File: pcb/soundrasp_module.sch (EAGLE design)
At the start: 65 parts, among them IC1 74HC165D, IC2 ULN2003AD, SW1 EC12E_SW, SW2 EC12E_SW

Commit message: Refactoring scema and doing initial pcb layout.
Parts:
- removed BACKLIGHT_LED, KNOB_LED: LED, SparkFun:LED-TRICOLOR-THROUGHHOLE
- removed C10, C12: 1uF, rcl:C-EUC0805
- removed IC2: ULN2003AD, uln-udn:ULN2003AD
- removed INDICATOR_SHIFT: 74HC595D, 74xx-eu:74HC595D
- removed JP1: (no value), SparkFun:M02LOCK_LONGPADS
- removed LED1, LED14, LED15, LED16, LED17, LED18, LED19, LED2: WS2812B, WS2812:WS2812B
- removed LED10, LED11, LED12, LED13, LED9: (no value), led:LEDCHIPLED_0805
- removed OS1, OS2: (no value), tcrt5000:TCRT5000
- removed R10, R11, R12, R13, R8, R9: (no value), rcl:R-EU_R0805
- removed R2, R3, R4, R5, R6, R7: 10k, rcl:R-EU_R0805
- removed R38, R41: 100k, rcl:R-EU_R0805
- removed R42, R43: 200 Ohm, rcl:R-EU_R0805
- removed R45, R46, R47, R48: 220, rcl:R-EU_R0805
- removed S1: (no value), SparkFun:TAC_SWITCHPTH
- removed SW2: EC12E_SW, switch-alps:EC12E_SW
- removed U$1: CHARACTER_LCD_8X2RT0802, character_lcd_RT0802B-1:CHARACTER_LCD_8X2RT0802
- added BAR1, BAR10, BAR2, BAR3, BAR4, BAR5, BAR6, BAR7, BAR8, BAR9, MODE_LED, TOGGLE_LED, WHEEL_LED: WS2812B, WS2812:WS2812B
- added DISPLAY: M16LOCK, SparkFun-Connectors:M16LOCK
- added FORCE_FEEDBACK: (no value), SparkFun:M02LOCK_LONGPADS
- added H1, H2, H3, H4: MOUNT-HOLE4.1, holes:MOUNT-HOLE4.1
- added IR_1, IR_2: (no value), SparkFun-LED:LED3MM
- added IR_SENSE_1, IR_SENSE_2: SFH205, opto-trans-siemens:SFH205
- added MENU_SWITCH, TOGGLE_SWITCH, WHEEL_SWITCH: SWITCH-MOMENTARY-2-SMD-1101NE, SparkFun-Electromechanical:SWITCH-MOMENTARY-2-SMD-1101NE
- added POWER_LED: (no value), led:LEDCHIPLED_0805
- added RN1: 220R, resistor-dil:4R-N0603-ARV
- added RN2, RN3: 10k, resistor-dil:4R-N0603-ARV
- added T1, T2: (no value), transistor:MMBT2222ALT1-NPN-SOT23-BEC
- R1: device pot:TRIM_EU-B25X -> rcl:R-TRIMM3296W
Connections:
- removed net N$14: BACKLIGHT_LED.RED, R8.2
- removed net N$18: KNOB_LED.BLU, R12.2
- removed net N$19: KNOB_LED.GRN, R13.2
- removed net N$24: INDICATOR_SHIFTA.QC, R10.1
- removed net N$25: INDICATOR_SHIFTA.QD, R11.1
- removed net N$29: LED1.DI, LED19.DO
- removed net N$74: OS2.ANODE, R42.2
- removed net N$75: INDICATOR_SHIFTA.SER, LCD_SHIFTA.QH*
- removed net N$76: INDICATOR_SHIFTA.QH*
- removed net N$79: OS1.ANODE, R43.2
- removed net N$81: INDICATOR_SHIFTA.QE, R12.1
- removed net N$82: INDICATOR_SHIFTA.QF, R13.1
- removed net N$83: IC2.I1, INDICATOR_SHIFTA.QG
- removed net N$84: IC2.I6, INDICATOR_SHIFTA.QH
- removed net N$85: IC2.I2, IC2.I3, LCD_SHIFTA.QG
- removed net N$88: IC2.I4, IC2.I5, LCD_SHIFTA.QH
- removed net N$89: IC2.O2, LED10.C
- removed net N$90: LED10.A, R45.1
- removed net N$91: IC2.O6, OS1.CATHODE, OS2.CATHODE
- removed net N$92: LED11.A, R46.1
- removed net N$93: IC2.O3, LED11.C
- removed net N$94: LED12.A, R47.1
- removed net N$95: LED13.A, R48.1
- removed net N$96: IC2.O4, LED12.C
- removed net N$97: IC2.O5, LED13.C
- removed net V+: R45.2, R46.2, R47.2, R48.2
- new net BAR7: BAR6.DO, BAR7.DI
- new net CONTRAST: DISPLAY.3, R1.S
- new net D4: DISPLAY.11, LCD_SHIFTA.QB
- new net D5: DISPLAY.12, LCD_SHIFTA.QC
- new net D6: DISPLAY.13, LCD_SHIFTA.QD
- new net D7: DISPLAY.14, LCD_SHIFTA.QE
- new net E: DISPLAY.6, LCD_SHIFTA.QA
- new net LED_COLORS_IN: TOGGLE_LED.DI, X1.5
- new net LED_COLORS_OUT: WHEEL_LED.DO, X2.5
- new net R/W: DISPLAY.5
- new net RS: DISPLAY.4, LCD_SHIFTA.QF
- net +5V: now also BAR1.VDD, BAR10.VDD, BAR2.VDD, BAR3.VDD, BAR4.VDD, BAR5.VDD, BAR6.VDD, BAR7.VDD, BAR8.VDD, BAR9.VDD, DISPLAY.15, DISPLAY.2, FORCE_FEEDBACK.1, MODE_LED.VDD, RN1C.1, RN1D.1, RN2A.2, RN2B.2, RN2C.2, RN2D.2, RN3A.2, RN3B.2, RN3C.2, RN3D.2, TOGGLE_LED.VDD, WHEEL_LED.VDD; no longer C10.1, C12.1, INDICATOR_SHIFTA.SCL, INDICATOR_SHIFTP.VCC, JP1.1, LED1.VDD, LED14.VDD, LED15.VDD, LED16.VDD, LED17.VDD, LED18.VDD, LED19.VDD, LED2.VDD, R2.2, R3.2, R38.2, R4.2, R41.2, R42.1, R43.1, R5.2, R6.2, R7.2, U$1.+5V
- net GND: now also BAR1.VSS, BAR10.VSS, BAR2.VSS, BAR3.VSS, BAR4.VSS, BAR5.VSS, BAR6.VSS, BAR7.VSS, BAR8.VSS, BAR9.VSS, DISPLAY.1, DISPLAY.16, IR_SENSE_1.C, IR_SENSE_2.C, MENU_SWITCH.1, MODE_LED.VSS, POWER_LED.C, T1.E, T2.E, TOGGLE_LED.VSS, TOGGLE_SWITCH.1, WHEEL_LED.VSS, WHEEL_SWITCH.1; no longer IC2.GND, INDICATOR_SHIFTA.G, INDICATOR_SHIFTP.GND, LED1.VSS, LED14.VSS, LED15.VSS, LED16.VSS, LED17.VSS, LED18.VSS, LED19.VSS, LED2.VSS, LED9.C, OS1.EMITTER, OS2.EMITTER, S1.2, SW2G$1.C, SW2G$2.2, U$1.GND, U$1.R/W
- net LED_VOLTAGE: no longer BACKLIGHT_LED.C, KNOB_LED.C, X1.5, X2.5
- net N$1: now also IR_1.A, RN1C.2; no longer R1.S, U$1.LCD_V+
- net N$10: now also BAR10.DI, BAR9.DO; no longer LCD_SHIFTA.QC, U$1.D5
- net N$11: now also BAR10.DO, WHEEL_LED.DI; no longer LCD_SHIFTA.QD, U$1.D6
- net N$12: now also MODE_LED.DI, TOGGLE_LED.DO; no longer LCD_SHIFTA.QE, U$1.D7
- net N$13: now also BAR1.DI, MODE_LED.DO; no longer LCD_SHIFTA.QF, U$1.RS
- net N$15: now also LCD_SHIFTA.QG, RN1A.1; no longer BACKLIGHT_LED.BLU, R9.2
- net N$16: now also RN1A.2, T1.B; no longer BACKLIGHT_LED.GRN, R10.2
- net N$17: now also LCD_SHIFTA.QH, RN1B.1; no longer KNOB_LED.RED, R11.2
- net N$2: now also RN2D.1; no longer R4.1
- net N$20: now also IR_1.C, IR_2.C, T2.C; no longer INDICATOR_SHIFTA.QA, R8.1
- net N$21: now also RN1B.2, T2.B; no longer INDICATOR_SHIFTA.QB, R9.1
- net N$22: now also BAR1.DO, BAR2.DI; no longer LED14.DO, LED15.DI
- net N$23: now also BAR2.DO, BAR3.DI; no longer LED15.DO, LED16.DI
- net N$26: now also BAR3.DO, BAR4.DI; no longer LED16.DO, LED17.DI
- net N$27: now also BAR4.DO, BAR5.DI; no longer LED17.DO, LED18.DI
- net N$28: now also BAR5.DO, BAR6.DI; no longer LED18.DO, LED19.DI
- net N$3: now also RN2C.1; no longer R5.1
- net N$30: now also BAR7.DO, BAR8.DI; no longer LED1.DO, LED2.DI
- net N$4: now also IR_SENSE_1.A, RN2A.1; no longer R6.1, SW2G$1.A
- net N$5: now also IR_SENSE_2.A, RN3D.1; no longer R7.1, SW2G$1.B
- net N$50: now also MENU_SWITCH.2, RN3B.1; no longer C10.2, OS2.COLLECTOR, R41.1
- net N$6: now also RN2B.1; no longer R2.1
- net N$7: now also RN3C.1, WHEEL_SWITCH.2; no longer R3.1, S1.4, SW2G$2.1
- net N$73: now also POWER_LED.A; no longer LED9.A
- net N$8: now also IR_2.A, RN1D.2; no longer LCD_SHIFTA.QA, U$1.ENABLE
- net N$80: now also RN3A.1, TOGGLE_SWITCH.2; no longer C12.2, OS1.COLLECTOR, R38.1
- net N$86: now also FORCE_FEEDBACK.2, T1.C; no longer IC2.O1, JP1.2
- net N$9: now also BAR8.DO, BAR9.DI; no longer LCD_SHIFTA.QB, U$1.D4
- net OUTPUT_CLOCK: no longer INDICATOR_SHIFTA.SCK
- net OUTPUT_LATCH: no longer INDICATOR_SHIFTA.RCK
- net OUTPUT_OUT: now also LCD_SHIFTA.QH*
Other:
- note added: "Character LCD display, 16x2"
- note added: "Mode Indicator"
- note added: "Optical Value Wheel"
- note added: "Power LED"
- note added: "Toggle Indicator"
- note added: "Value Indicator Bar"
- note added: "Wheel Light"
- note removed: "Backlight"
- note removed: "Edge Lighting"
- note removed: "Knob Light"
- note removed: "LCD 8x2"
- note removed: "Position Indicators"
- note removed: "Powerled"
- note removed: "Proximity Sensors"
- note removed: "Value Knob"
- moved on the sheet: C11, D1, IC1, IC1P, LCD_SHIFTP, R39, R40, R44, SW1, X1, X2

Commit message: Removed force feedback. Changed design to use one common IR LED.
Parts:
- removed C11: 1nF, rcl:C-EUC0805
- removed D1: (no value), SparkFun:DIODEPTH
- removed FORCE_FEEDBACK: (no value), SparkFun:M02LOCK_LONGPADS
- removed IR_2: (no value), SparkFun-LED:LED3MM
- removed R44: 100 Ohm, rcl:R-EU_R0805
- removed T1, T2: (no value), transistor:MMBT2222ALT1-NPN-SOT23-BEC
- removed X1: (no value), SparkFun:DB9MALE
- removed X2: (no value), SparkFun:DB9FEMALE
- added JP1, JP2: M09LOCK-LONGPADS, SparkFun:M09LOCK-LONGPADS
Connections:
- removed net N$16: RN1A.2, T1.B
- removed net N$17: LCD_SHIFTA.QH, RN1B.1
- removed net N$20: IR_1.C, IR_2.C, T2.C
- removed net N$21: RN1B.2, T2.B
- removed net N$8: IR_2.A, RN1D.2
- removed net N$86: C11.2, D1.A, FORCE_FEEDBACK.2, T1.C
- removed net N$87: C11.1, R44.1
- net +5V: now also JP1.9, JP2.9; no longer D1.C, FORCE_FEEDBACK.1, R44.2, RN1D.1, X1.9, X2.9
- net GND: now also JP1.1, JP2.1; no longer T1.E, T2.E, X1.1, X2.1
- net INPUT_CLOCK: now also JP1.7, JP2.7; no longer X1.7, X2.7
- net INPUT_IN: now also JP2.6; no longer X2.6
- net INPUT_LATCH: now also JP1.8, JP2.8; no longer X1.8, X2.8
- net INPUT_OUT: now also JP1.6; no longer X1.6
- net LED_COLORS_IN: now also JP1.5; no longer X1.5
- net LED_COLORS_OUT: now also JP2.5; no longer X2.5
- net N$15: now also IR_1.C; no longer RN1A.1
- net OUTPUT_CLOCK: now also JP1.3, JP2.3; no longer X1.3, X2.3
- net OUTPUT_IN: now also JP1.2; no longer X1.2
- net OUTPUT_LATCH: now also JP1.4, JP2.4; no longer X1.4, X2.4
- net OUTPUT_OUT: now also JP2.2; no longer X2.2
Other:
- note removed: "Force Feedback"
- moved on the sheet: DISPLAY, IR_1, IR_SENSE_1, LCD_SHIFT, LCD_SHIFTP, R1, RN1C

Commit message: Tuned schema and board.
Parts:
- removed C4, C5, C6, C9: 100nF, rcl:C-EUC0805
- removed RN1: 220R, resistor-dil:4R-N0603-ARV
- added R2: 220R, rcl:R-EU_R0805
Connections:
- removed net LED_VOLTAGE: C7.+, C8.+, C9.1
- net +5V: now also C7.+, C8.+, R2.2; no longer C4.1, C5.1, C6.1, RN1C.1
- net GND: no longer C4.2, C5.2, C6.2, C9.2
- net N$1: now also R2.1; no longer RN1C.2
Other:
- note added: "TODO: Control display backlight with QG, IR led with QH"
- note added: "TODO: Do we need toggle indicator? And toggle button?"
- moved on the sheet: C7, C8

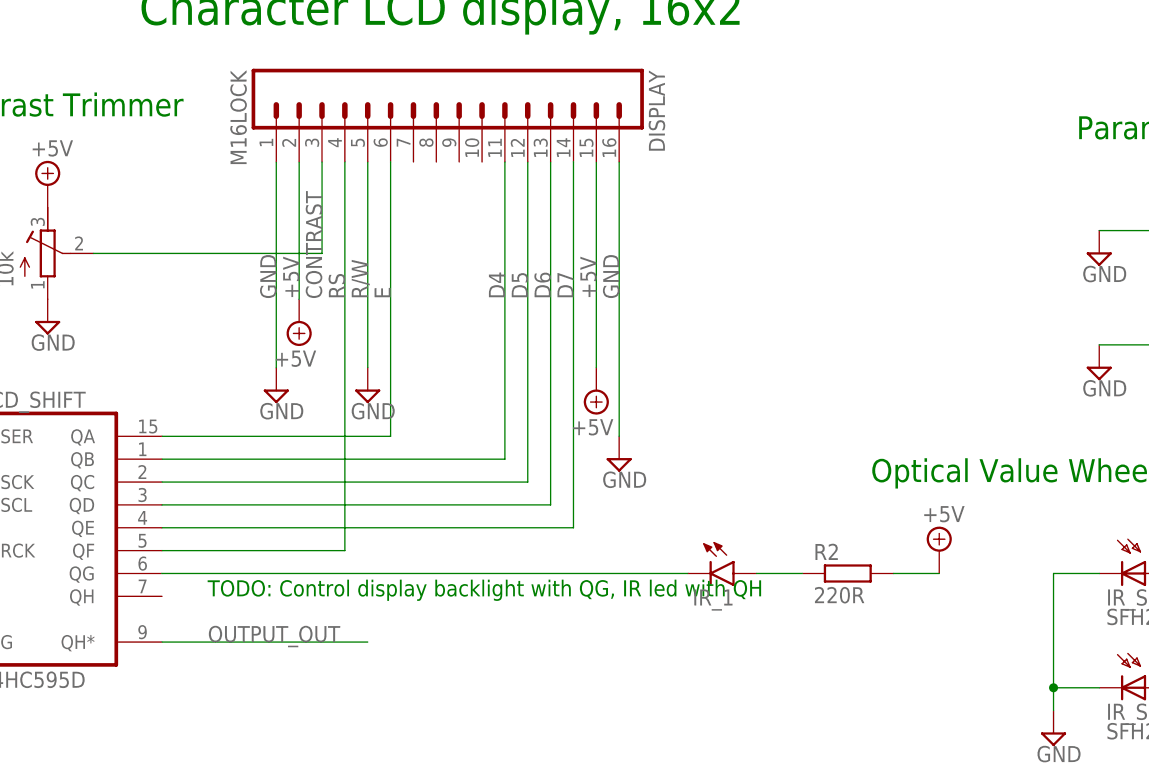
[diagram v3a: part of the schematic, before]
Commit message: Made LCD backlight controllable.
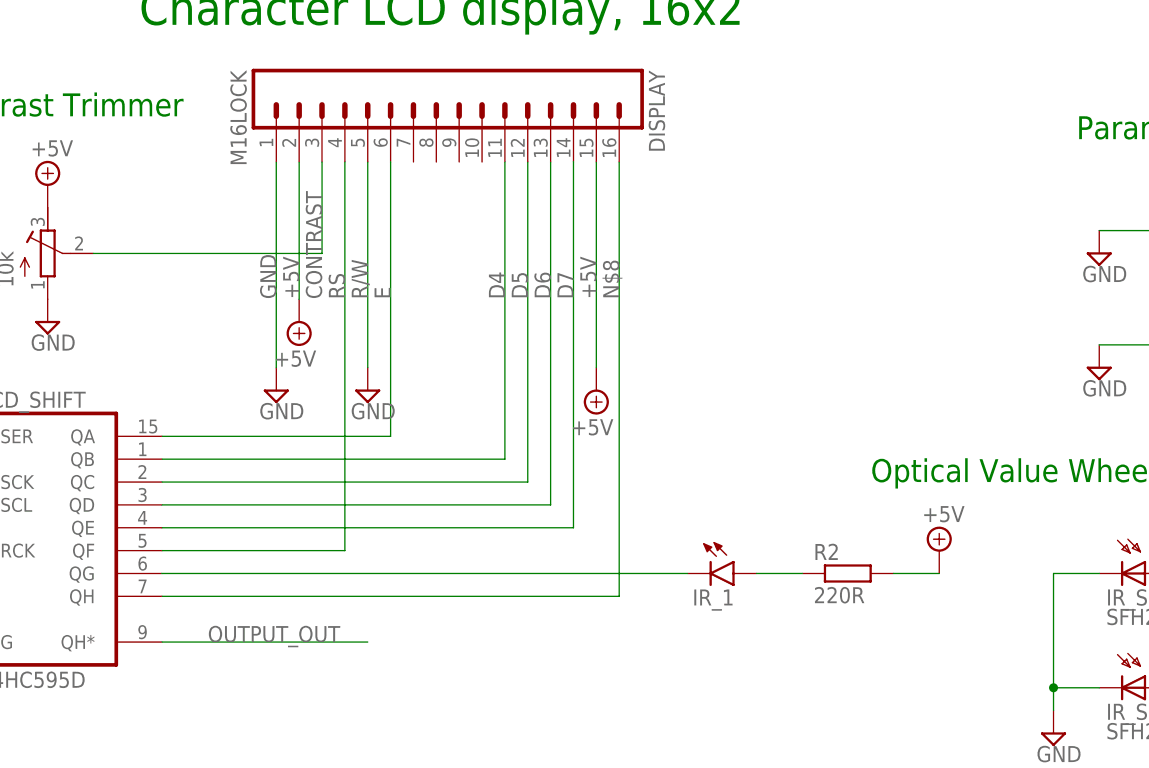
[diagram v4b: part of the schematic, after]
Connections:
- new net N$8: DISPLAY.16, LCD_SHIFTA.QH
- net GND: no longer DISPLAY.16
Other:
- note removed: "TODO: Control display backlight with QG, IR led with QH"
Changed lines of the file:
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@@
 <part name="SUPPLY41" library="supply2" deviceset="+5V" device=""/>
 <part name="SUPPLY58" library="supply2" deviceset="GND" device=""/>
-<part name="SUPPLY51" library="supply2" deviceset="GND" device=""/>
 <part name="SUPPLY52" library="supply2" deviceset="+5V" device=""/>
 <part name="IR_1" library="SparkFun-LED" deviceset="LED" device="3MM"/>
@@
 <text x="-43.18" y="60.96" size="3.81" layer="91">Character LCD display, 16x2</text>
 <text x="-231.14" y="-106.68" size="2.54" layer="91">Toggle Indicator</text>
-<text x="-35.56" y="-2.54" size="1.778" layer="91">TODO: Control display backlight with QG, IR led with QH</text>
 <text x="-228.6" y="-96.52" size="1.778" layer="91">TODO: Do we need toggle indicator?  And toggle button?</text>
 </plain>
@@
 <instance part="SUPPLY41" gate="+5V" x="-25.4" y="27.94" rot="R180"/>
 <instance part="SUPPLY58" gate="GND" x="-17.78" y="20.32"/>
-<instance part="SUPPLY51" gate="GND" x="10.16" y="12.7"/>
 <instance part="SUPPLY52" gate="+5V" x="7.62" y="20.32" rot="R180"/>
 <instance part="IR_1" gate="G$1" x="22.86" y="0" rot="R270"/>
@@
 </segment>
 <segment>
-<pinref part="DISPLAY" gate="G$1" pin="16"/>
-<pinref part="SUPPLY51" gate="GND" pin="GND"/>
-<wire x1="10.16" y1="15.24" x2="10.16" y2="45.72" width="0.1524" layer="91"/>
-<label x="10.16" y="30.48" size="1.778" layer="95" rot="R90"/>
-</segment>
-<segment>
 <pinref part="TOGGLE_LED" gate="G$1" pin="VSS"/>
 <pinref part="SUPPLY21" gate="GND" pin="GND"/>
@@
 </segment>
 </net>
+<net name="N$8" class="0">
+<segment>
+<pinref part="DISPLAY" gate="G$1" pin="16"/>
+<wire x1="10.16" y1="-2.54" x2="10.16" y2="45.72" width="0.1524" layer="91"/>
+<label x="10.16" y="30.48" size="1.778" layer="95" rot="R90"/>
+<pinref part="LCD_SHIFT" gate="A" pin="QH"/>
+<wire x1="-40.64" y1="-2.54" x2="10.16" y2="-2.54" width="0.1524" layer="91"/>
+</segment>
+</net>
